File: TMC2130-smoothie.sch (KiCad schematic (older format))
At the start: 4 parts, among them P1 CONN_01X04, P2 CONN_01X04, P3 CONN_01X04, P4 CONN_01X04

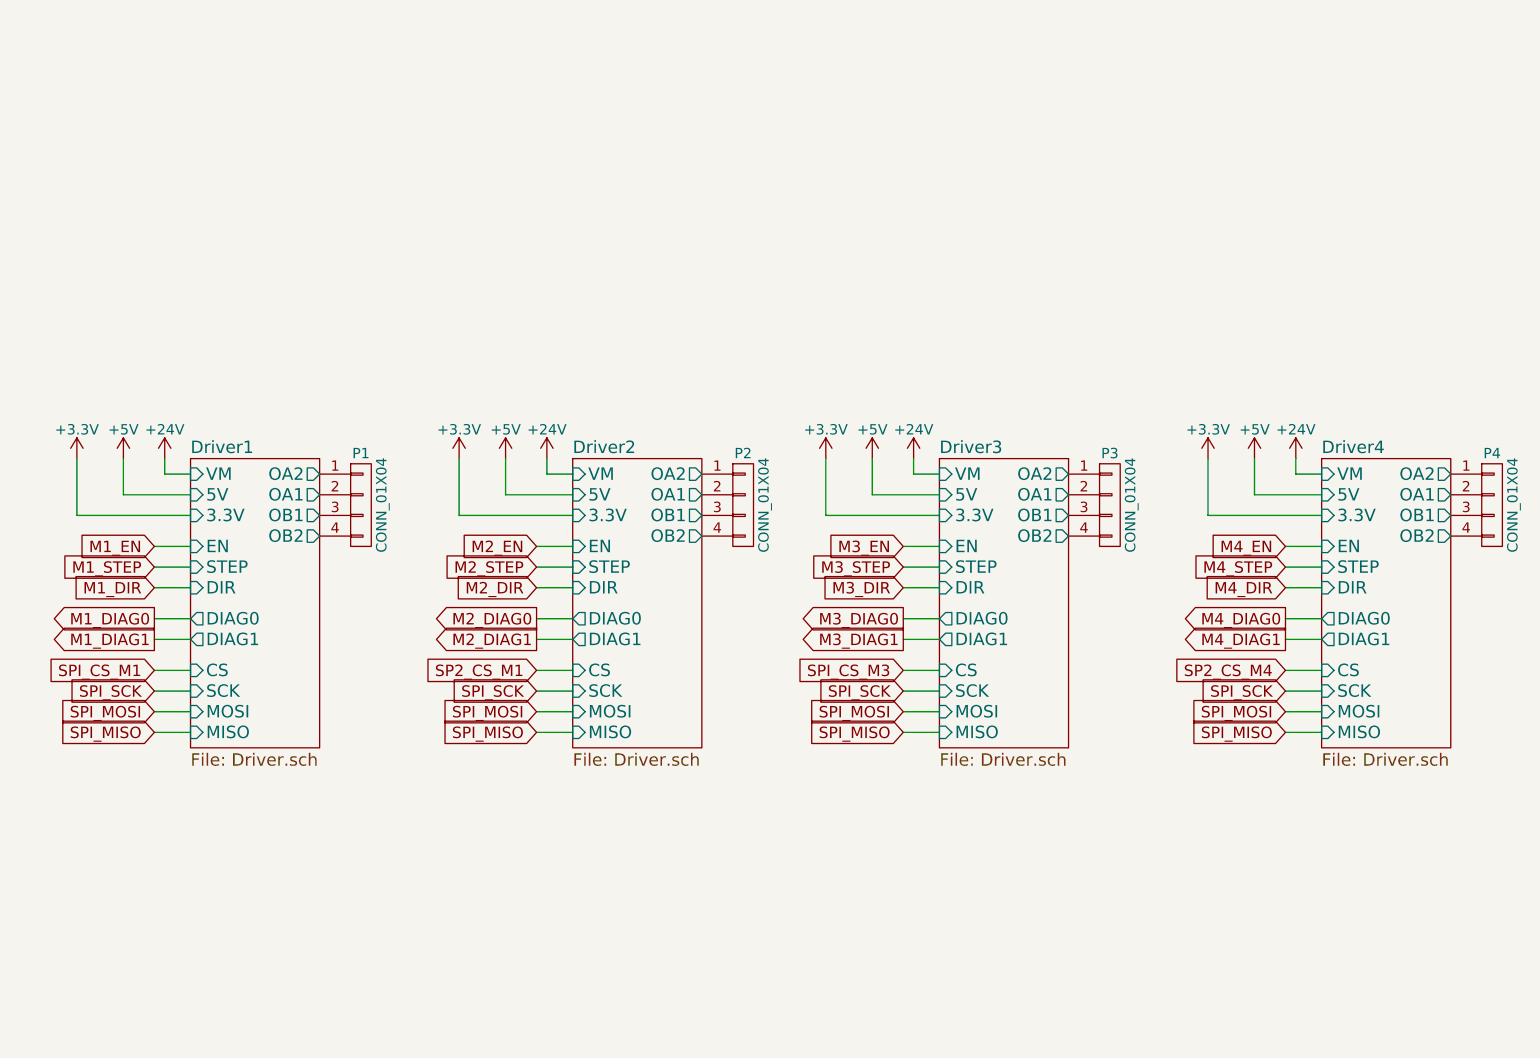
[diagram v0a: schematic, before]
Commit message: Initial layout of 1-driver
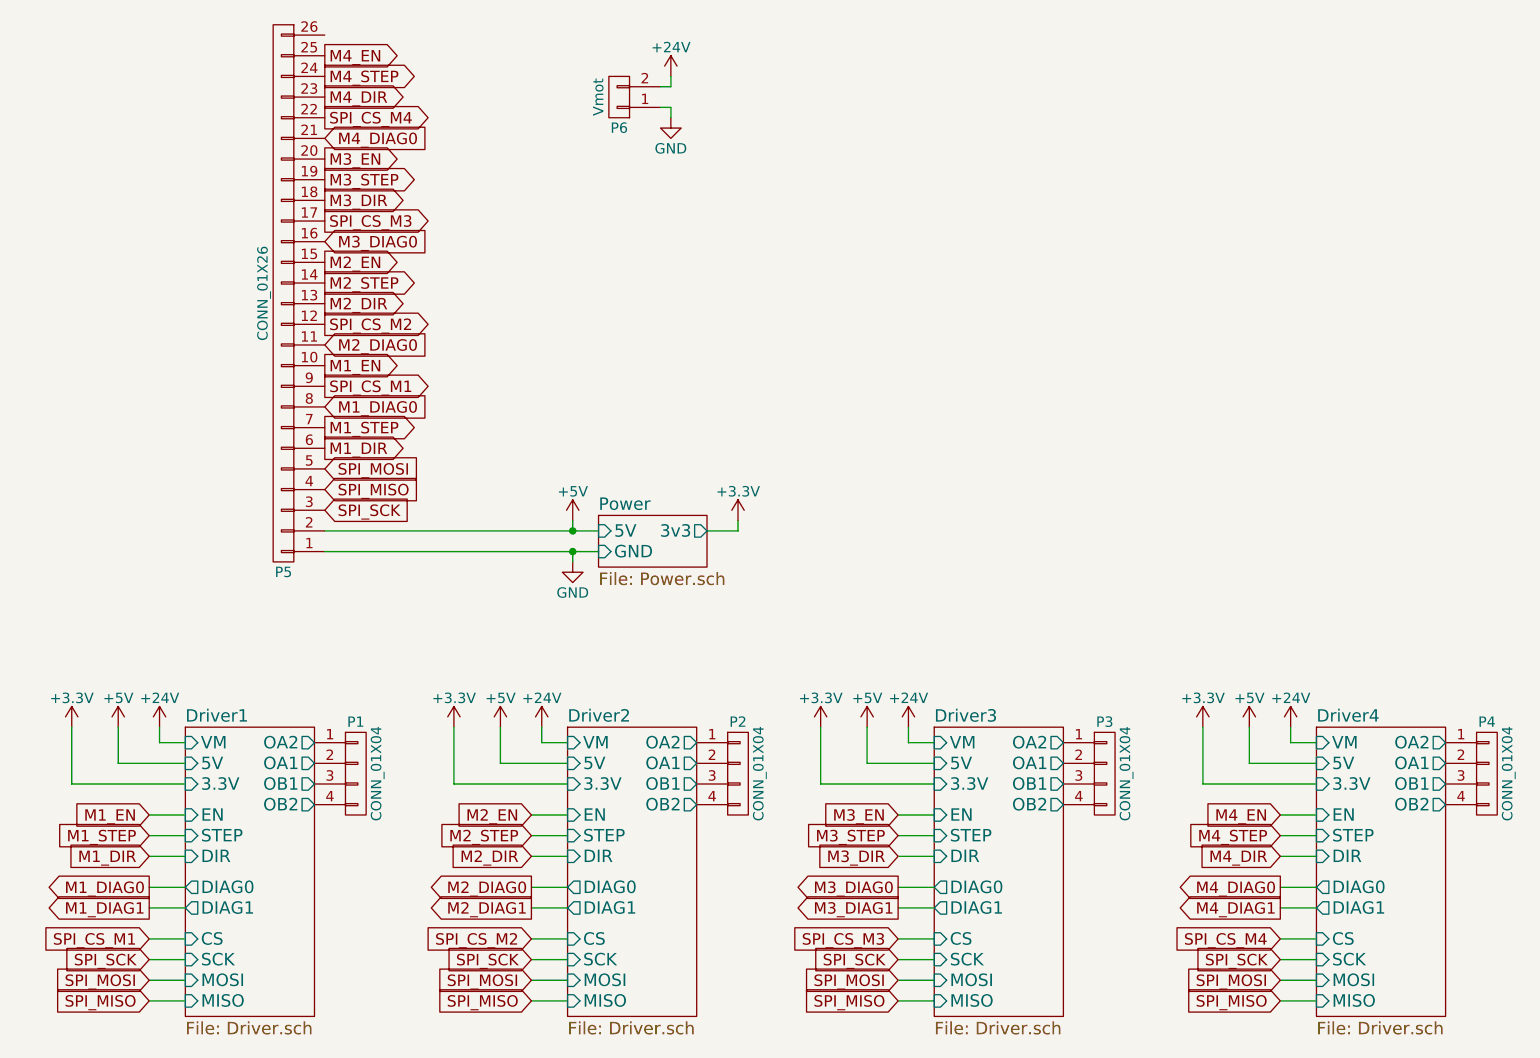
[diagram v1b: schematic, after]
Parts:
- added P5: CONN_01X26, Pin_Headers:Pin_Header_Straight_2x13_Pitch1.27mm_SMD, symbol CONN_01X26
- added P6: Vmot, Connect:AK300-2, symbol CONN_01X02
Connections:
- net +24V: now also P6.2 (P2)
- net +5V: now also P5.2 (P2)
- net M1_DIAG0: now also P5.8 (P8)
- net M1_DIR: now also P5.6 (P6)
- net M1_EN: now also P5.10 (P10)
- net M1_STEP: now also P5.7 (P7)
- net M2_DIAG0: now also P5.11 (P11)
- net M2_DIR: now also P5.13 (P13)
- net M2_EN: now also P5.15 (P15)
- net M2_STEP: now also P5.14 (P14)
- net M3_DIAG0: now also P5.16 (P16)
- net M3_DIR: now also P5.18 (P18)
- net M3_EN: now also P5.20 (P20)
- net M3_STEP: now also P5.19 (P19)
- net M4_DIAG0: now also P5.21 (P21)
- net M4_DIR: now also P5.23 (P23)
- net M4_EN: now also P5.25 (P25)
- net M4_STEP: now also P5.24 (P24)
- net SPI_CS_M1: now also P5.9 (P9)
- net SPI_CS_M3: now also P5.17 (P17)
- net SPI_MISO: now also P5.4 (P4)
- net SPI_MOSI: now also P5.5 (P5)
- net SPI_SCK: now also P5.3 (P3)
- new net GND: P5.1 (P1), P6.1 (P1)
- new net SPI_CS_M2: P5.12 (P12)
- new net SPI_CS_M4: P5.22 (P22)
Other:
- moved on the sheet: P1, P2, P3, P4

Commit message: Routed entire PCB
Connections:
- net M2_DIAG0: now also P5.13 (P13); no longer P5.11 (P11)
- net M2_DIR: now also P5.14 (P14); no longer P5.13 (P13)
- net M2_STEP: now also P5.11 (P11); no longer P5.14 (P14)
- net M3_DIAG0: now also P5.19 (P19); no longer P5.16 (P16)
- net M3_STEP: now also P5.17 (P17); no longer P5.19 (P19)
- net M4_DIAG0: now also P5.24 (P24); no longer P5.21 (P21)
- net M4_STEP: now also P5.21 (P21); no longer P5.24 (P24)
- net SPI_CS_M3: now also P5.16 (P16); no longer P5.17 (P17)
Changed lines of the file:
@@
 Text GLabel 3800 2175 2    55   Output ~ 0
 M2_EN
+Text GLabel 3800 2575 2    55   Output ~ 0
+M2_STEP
 Text GLabel 3800 2275 2    55   Output ~ 0
-M2_STEP
-Text GLabel 3800 2375 2    55   Output ~ 0
 M2_DIR
-Text GLabel 3800 2575 2    55   Input ~ 0
+Text GLabel 3800 2375 2    55   Input ~ 0
 M2_DIAG0
 Text GLabel 3800 2475 2    55   Output ~ 0
@@
 Text GLabel 3800 1675 2    55   Output ~ 0
 M3_EN
-Text GLabel 3800 1775 2    55   Output ~ 0
+Text GLabel 3800 1975 2    55   Output ~ 0
 M3_STEP
 Text GLabel 3800 1875 2    55   Output ~ 0
 M3_DIR
-Text GLabel 3800 1975 2    55   Output ~ 0
+Text GLabel 3800 2075 2    55   Output ~ 0
 SPI_CS_M3
-Text GLabel 3800 2075 2    55   Input ~ 0
+Text GLabel 3800 1775 2    55   Input ~ 0
 M3_DIAG0
 Text GLabel 3800 1175 2    55   Output ~ 0
 M4_EN
-Text GLabel 3800 1275 2    55   Output ~ 0
+Text GLabel 3800 1575 2    55   Output ~ 0
 M4_STEP
 Text GLabel 3800 1375 2    55   Output ~ 0
 M4_DIR
-Text GLabel 3800 1575 2    55   Input ~ 0
+Text GLabel 3800 1275 2    55   Input ~ 0
 M4_DIAG0
 Text GLabel 3800 1475 2    55   Output ~ 0
@@
 	8050 4425 8050 4700
 $Comp
-L +3.3V #PWR017
+L +3.3V #PWR09
 U 1 1 59D73565
 P 8050 4425
-F 0 "#PWR017" H 8050 4275 50  0001 C CNN
+F 0 "#PWR09" H 8050 4275 50  0001 C CNN
 F 1 "+3.3V" H 8050 4565 50  0000 C CNN
 F 2 "" H 8050 4425 50  0000 C CNN
@@
 	8275 4425 8275 4600
 $Comp
-L +5V #PWR016
+L +5V #PWR010
 U 1 1 59D7355D
 P 8275 4425
-F 0 "#PWR016" H 8275 4275 50  0001 C CNN
+F 0 "#PWR010" H 8275 4275 50  0001 C CNN
 F 1 "+5V" H 8275 4565 50  0000 C CNN
 F 2 "" H 8275 4425 50  0000 C CNN
@@
 	8475 4425 8475 4500
 $Comp
-L +24V #PWR015
+L +24V #PWR011
 U 1 1 59D73555
 P 8475 4425
-F 0 "#PWR015" H 8475 4275 50  0001 C CNN
+F 0 "#PWR011" H 8475 4275 50  0001 C CNN
 F 1 "+24V" H 8475 4565 50  0000 C CNN
 F 2 "" H 8475 4425 50  0000 C CNN
@@
 	6200 4425 6200 4700
 $Comp
-L +3.3V #PWR014
+L +3.3V #PWR012
 U 1 1 59D73523
 P 6200 4425
-F 0 "#PWR014" H 6200 4275 50  0001 C CNN
+F 0 "#PWR012" H 6200 4275 50  0001 C CNN
 F 1 "+3.3V" H 6200 4565 50  0000 C CNN
 F 2 "" H 6200 4425 50  0000 C CNN
@@
 	6625 4425 6625 4500
 $Comp
-L +24V #PWR012
+L +24V #PWR014
 U 1 1 59D73513
 P 6625 4425
-F 0 "#PWR012" H 6625 4275 50  0001 C CNN
+F 0 "#PWR014" H 6625 4275 50  0001 C CNN
 F 1 "+24V" H 6625 4565 50  0000 C CNN
 F 2 "" H 6625 4425 50  0000 C CNN
@@
 	4425 4425 4425 4700
 $Comp
-L +3.3V #PWR011
+L +3.3V #PWR015
 U 1 1 59D6DDB9
 P 4425 4425
-F 0 "#PWR011" H 4425 4275 50  0001 C CNN
+F 0 "#PWR015" H 4425 4275 50  0001 C CNN
 F 1 "+3.3V" H 4425 4565 50  0000 C CNN
 F 2 "" H 4425 4425 50  0000 C CNN
@@
 	4650 4425 4650 4600
 $Comp
-L +5V #PWR010
+L +5V #PWR016
 U 1 1 59D6DDB1
 P 4650 4425
-F 0 "#PWR010" H 4650 4275 50  0001 C CNN
+F 0 "#PWR016" H 4650 4275 50  0001 C CNN
 F 1 "+5V" H 4650 4565 50  0000 C CNN
 F 2 "" H 4650 4425 50  0000 C CNN
@@
 	4850 4425 4850 4500
 $Comp
-L +24V #PWR09
+L +24V #PWR017
 U 1 1 59D6DDA9
 P 4850 4425
-F 0 "#PWR09" H 4850 4275 50  0001 C CNN
+F 0 "#PWR017" H 4850 4275 50  0001 C CNN
 F 1 "+24V" H 4850 4565 50  0000 C CNN
 F 2 "" H 4850 4425 50  0000 C CNN
